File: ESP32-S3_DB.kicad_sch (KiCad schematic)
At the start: 0 parts

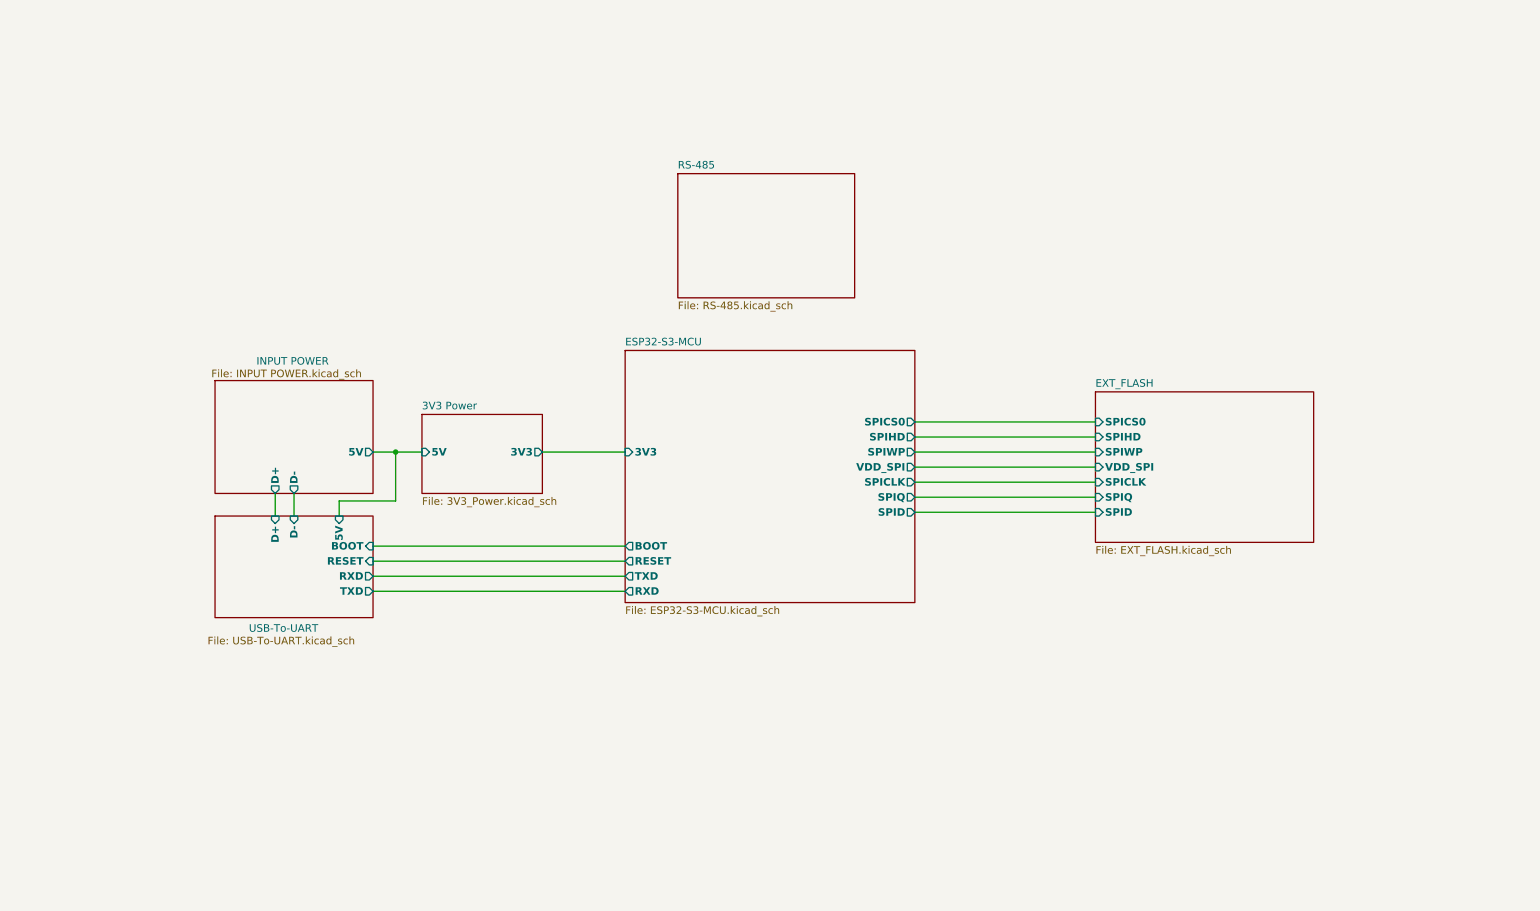
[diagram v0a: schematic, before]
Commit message: Completed RS-485 connections
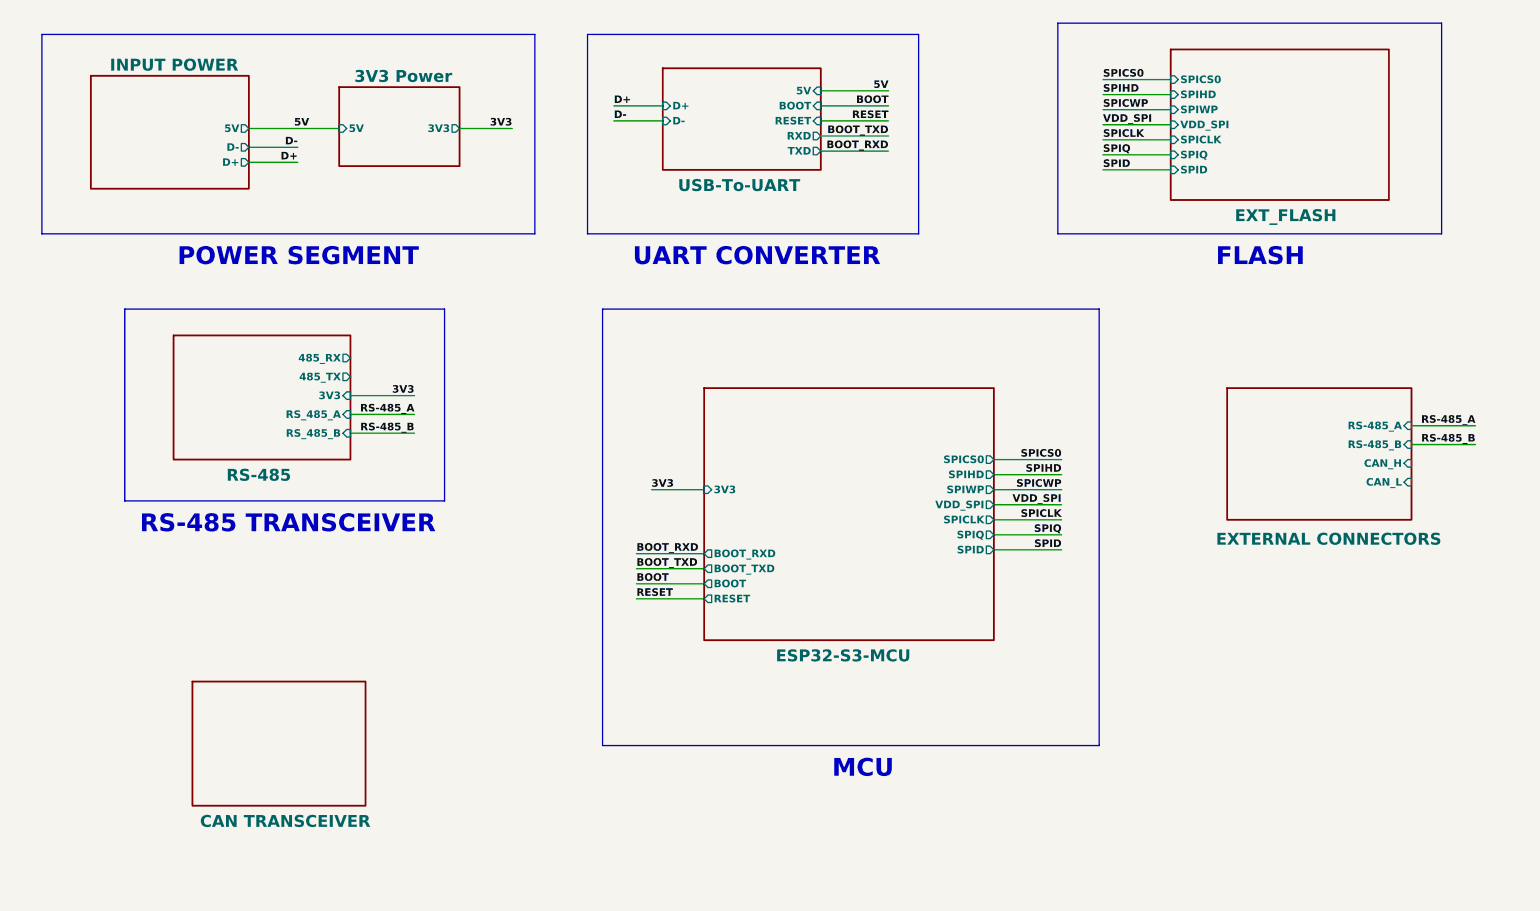
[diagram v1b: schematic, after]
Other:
- added sheet CAN TRANSCEIVER (CAN-TRANSCEIVER.kicad_sch)
- added sheet EXTERNAL CONNECTORS (External_connec.kicad_sch)
- sheet ESP32-S3-MCU ports: added BOOT_RXD, BOOT_TXD; removed RXD, TXD
- sheet RS-485 ports: added 3V3, 485_RX, 485_TX, RS_485_A, RS_485_B; removed none
- note added: "FLASH"
- note added: "MCU"
- note added: "POWER SEGMENT"
- note added: "RS-485 TRANSCEIVER"
- note added: "UART CONVERTER"

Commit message: Added CAN Transceiver
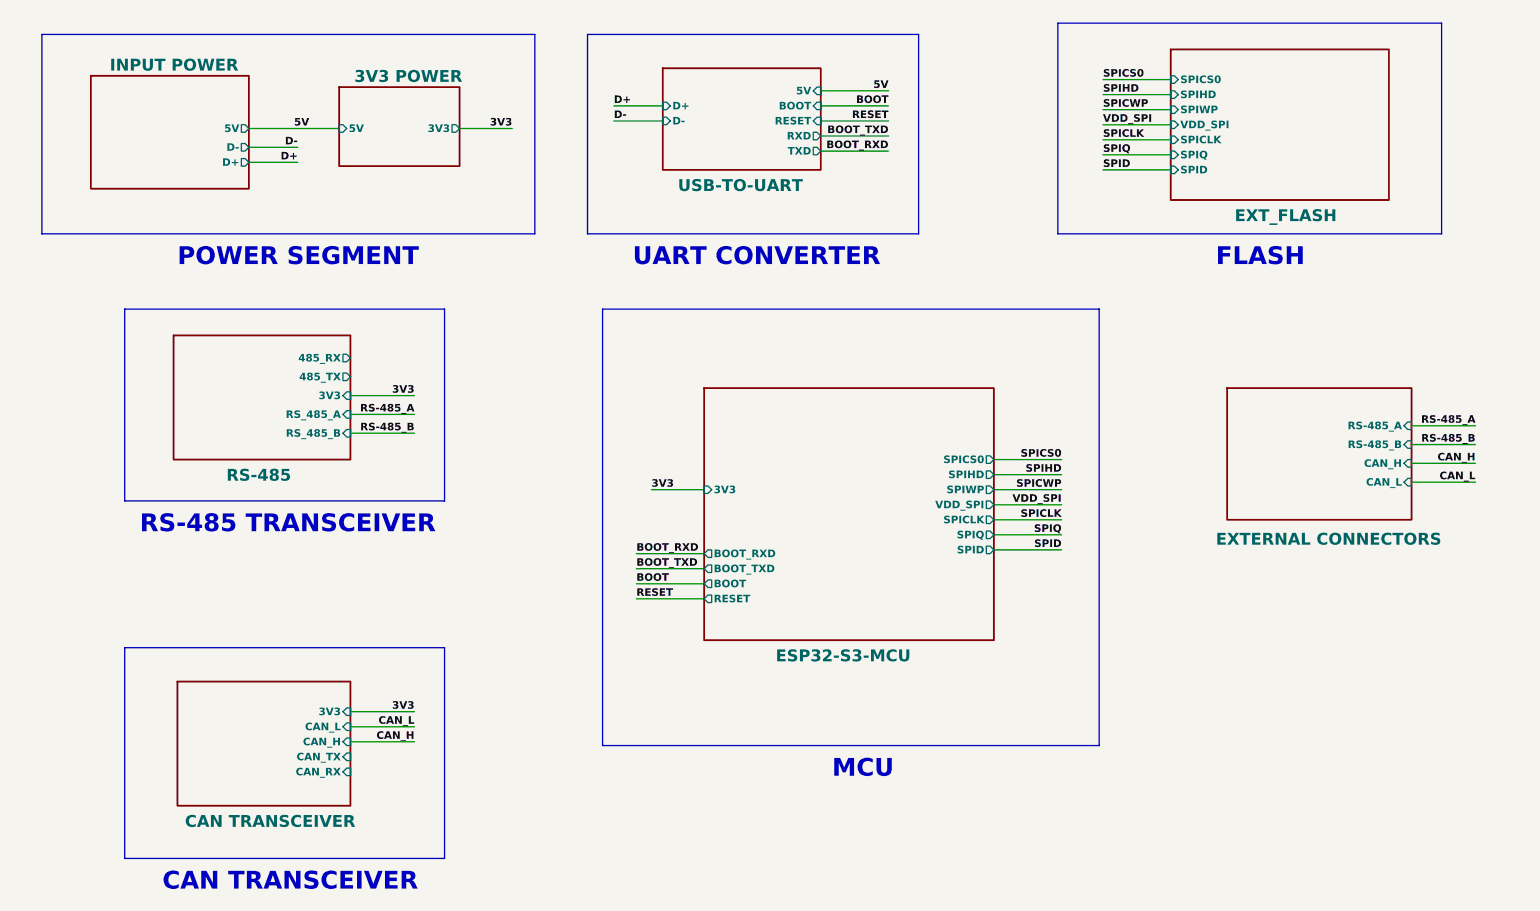
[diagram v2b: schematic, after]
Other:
- sheet 3V3 Power renamed 3V3 POWER
- sheet USB-To-UART renamed USB-TO-UART
- sheet CAN TRANSCEIVER ports: added 3V3, CAN_H, CAN_L, CAN_RX, CAN_TX; removed none
- note added: "CAN TRANSCEIVER"
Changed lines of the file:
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@@
+    (stroke (width 1) (type default) (color 72 72 72 1))
+  )
+  (bus (pts (xy 40.64 125.095) (xy 40.64 160.655))
     (stroke (width 1) (type default) (color 72 72 72 1))
   )
@@
     (stroke (width 1) (type default) (color 72 72 72 1))
   )
+  (wire (pts (xy 78.74 140.97) (xy 89.535 140.97))
+    (stroke (width 0.5) (type default) (color 0 0 0 1))
+  )
   (wire (pts (xy 61.595 43.18) (xy 69.85 43.18))
     (stroke (width 0.5) (type default) (color 0 0 255 1))
@@
   )
   (bus (pts (xy 121.285 67.945) (xy 205.105 67.945))
+    (stroke (width 1) (type default) (color 72 72 72 1))
+  )
+  (bus (pts (xy 40.64 125.095) (xy 94.615 125.095))
     (stroke (width 1) (type default) (color 72 72 72 1))
   )
@@
     (stroke (width 0.5) (type default) (color 255 0 0 1))
   )
+  (bus (pts (xy 94.615 160.655) (xy 40.64 160.655))
+    (stroke (width 1) (type default) (color 72 72 72 1))
+  )
+  (bus (pts (xy 94.615 125.095) (xy 94.615 160.655))
+    (stroke (width 1) (type default) (color 72 72 72 1))
+  )
+  (wire (pts (xy 78.74 138.43) (xy 89.535 138.43))
+    (stroke (width 0.5) (type default) (color 0 0 0 1))
+  )
   (wire (pts (xy 123.19 36.195) (xy 131.445 36.195))
     (stroke (width 0.5) (type default) (color 0 0 255 1))
@@
     (stroke (width 0.5) (type default) (color 0 0 255 1))
   )
+  (wire (pts (xy 257.81 97.155) (xy 268.605 97.155))
+    (stroke (width 0.5) (type default) (color 0 0 0 1))
+  )
+  (wire (pts (xy 78.74 135.89) (xy 89.535 135.89))
+    (stroke (width 0.5) (type default) (color 255 0 0 1))
+  )
   (wire (pts (xy 217.17 39.37) (xy 205.74 39.37))
     (stroke (width 0.5) (type default) (color 0 0 255 1))
@@
   (wire (pts (xy 217.17 36.83) (xy 205.74 36.83))
     (stroke (width 0.5) (type default) (color 0 0 255 1))
+  )
+  (wire (pts (xy 257.81 93.98) (xy 268.605 93.98))
+    (stroke (width 0.5) (type default) (color 0 0 0 1))
   )
   (bus (pts (xy 262.89 55.245) (xy 198.12 55.245))
@@
     (effects (font (size 3 3) bold (color 255 0 0 1)) (justify left bottom))
   )
+  (text "CAN TRANSCEIVER" (at 46.99 166.37 0)
+    (effects (font (size 3 3) bold (color 255 0 0 1)) (justify left bottom))
+  )
   (text "RS-485 TRANSCEIVER" (at 43.18 106.045 0)
     (effects (font (size 3 3) bold (color 255 0 0 1)) (justify left bottom))
@@
     (effects (font (size 1.27 1.27) bold (color 0 0 255 1)) (justify left bottom))
   )
+  (label "3V3" (at 89.535 135.89 180) (fields_autoplaced)
+    (effects (font (size 1.27 1.27) bold (color 255 0 0 1)) (justify right bottom))
+  )
   (label "BOOT_RXD" (at 127 109.22 0) (fields_autoplaced)
     (effects (font (size 1.27 1.27) bold (color 0 0 255 1)) (justify left bottom))
@@
     (effects (font (size 1.27 1.27) bold (color 132 0 0 1)) (justify left bottom))
   )
+  (label "CAN_H" (at 268.605 93.98 180) (fields_autoplaced)
+    (effects (font (size 1.27 1.27) bold (color 0 0 0 1)) (justify right bottom))
+  )
+  (label "CAN_L" (at 268.605 97.155 180) (fields_autoplaced)
+    (effects (font (size 1.27 1.27) bold (color 0 0 0 1)) (justify right bottom))
+  )
   (label "D-" (at 123.19 36.195 0) (fields_autoplaced)
     (effects (font (size 1.27 1.27) bold (color 0 0 255 1)) (justify left bottom))
@@
     (effects (font (size 1.27 1.27) bold (color 0 194 0 1)) (justify left bottom))
   )
+  (label "CAN_H" (at 89.535 140.97 180) (fields_autoplaced)
+    (effects (font (size 1.27 1.27) bold (color 0 0 0 1)) (justify right bottom))
+  )
   (label "SPIQ" (at 198.755 106.045 180) (fields_autoplaced)
     (effects (font (size 1.27 1.27) bold (color 0 0 255 1)) (justify right bottom))
@@
     (effects (font (size 1.27 1.27) bold (color 0 0 255 1)) (justify left bottom))
   )
+  (label "CAN_L" (at 89.535 138.43 180) (fields_autoplaced)
+    (effects (font (size 1.27 1.27) bold (color 0 0 0 1)) (justify right bottom))
+  )
   (sheet (at 217.17 24.13) (size 36.83 25.4)
     (stroke (width 0.3) (type solid) (color 0 0 0 1))
     (fill (color 255 255 194 1.0000))
     (property "Sheetname" "EXT_FLASH" (at 227.965 53.34 0)
-      (effects (font (size 2 2) bold) (justify left bottom))
+      (effects (font (size 2 2) bold (color 0 0 0 1)) (justify left bottom))
     )
     (property "Sheetfile" "EXT_FLASH.kicad_sch" (at 217.17 50.1146 0)
@@
     )
   )
-  (sheet (at 52.07 130.81) (size 29.21 20.955)
-    (stroke (width 0.3) (type solid) (color 0 0 0 1))
-    (fill (color 255 255 194 1.0000))
-    (property "Sheetname" "CAN TRANSCEIVER" (at 53.34 155.575 0)
-      (effects (font (size 2 2) bold) (justify left bottom))
-    )
-    (property "Sheetfile" "CAN-TRANSCEIVER.kicad_sch" (at 52.07 152.4234 0)
-      (effects (font (size 1.27 1.27)) (justify left top) hide)
+  (sheet (at 49.53 130.81) (size 29.21 20.955)
+    (stroke (width 0.3) (type solid) (color 0 0 0 1))
+    (fill (color 255 255 194 1.0000))
+    (property "Sheetname" "CAN TRANSCEIVER" (at 50.8 155.575 0)
+      (effects (font (size 2 2) bold (color 0 0 0 1)) (justify left bottom))
+    )
+    (property "Sheetfile" "CAN-TRANSCEIVER.kicad_sch" (at 49.53 152.4234 0)
+      (effects (font (size 1.27 1.27)) (justify left top) hide)
+    )
+    (pin "CAN_L" input (at 78.74 138.43 0)
+      (effects (font (size 1.27 1.27) (thickness 0.254) bold (color 0 0 0 1)) (justify right))
+    )
+    (pin "3V3" input (at 78.74 135.89 0)
+      (effects (font (size 1.27 1.27) (thickness 0.254) bold (color 255 0 0 1)) (justify right))
+    )
+    (pin "CAN_H" input (at 78.74 140.97 0)
+      (effects (font (size 1.27 1.27) (thickness 0.254) bold (color 0 0 0 1)) (justify right))
+    )
+    (pin "CAN_TX" input (at 78.74 143.51 0)
+      (effects (font (size 1.27 1.27) (thickness 0.254) bold (color 0 0 255 1)) (justify right))
+    )
+    (pin "CAN_RX" input (at 78.74 146.05 0)
+      (effects (font (size 1.27 1.27) (thickness 0.254) bold (color 0 0 255 1)) (justify right))
     )
     (instances
@@
     (fill (color 255 255 194 1.0000))
     (property "Sheetname" "INPUT POWER" (at 38.1 27.94 0)
-      (effects (font (size 2 2) bold) (justify left bottom))
+      (effects (font (size 2 2) bold (color 0 0 0 1)) (justify left bottom))
     )
     (property "Sheetfile" "INPUT POWER.kicad_sch" (at 34.29 48.26 0)
@@
     (fill (color 255 255 194 1.0000))
     (property "Sheetname" "RS-485" (at 57.785 97.155 0)
-      (effects (font (size 2 2) bold) (justify left bottom))
+      (effects (font (size 2 2) bold (color 0 0 0 1)) (justify left bottom))
     )
     (property "Sheetfile" "RS-485.kicad_sch" (at 48.895 93.9296 0)
@@
     (stroke (width 0.3) (type solid) (color 0 0 0 1))
     (fill (color 255 255 194 1.0000))
-    (property "Sheetname" "USB-To-UART" (at 133.985 48.26 0)
-      (effects (font (size 2 2) bold) (justify left bottom))
+    (property "Sheetname" "USB-TO-UART" (at 133.985 48.26 0)
+      (effects (font (size 2 2) bold (color 0 0 0 1)) (justify left bottom))
     )
     (property "Sheetfile" "USB-To-UART.kicad_sch" (at 130.175 47.625 0)
@@
     (fill (color 255 255 194 1.0000))
     (property "Sheetname" "ESP32-S3-MCU" (at 150.495 127.635 0)
-      (effects (font (size 2 2) bold) (justify left bottom))
+      (effects (font (size 2 2) bold (color 0 0 0 1)) (justify left bottom))
     )
     (property "Sheetfile" "ESP32-S3-MCU.kicad_sch" (at 138.43 124.4096 0)
@@
     (fill (color 255 255 194 1.0000))
     (property "Sheetname" "EXTERNAL CONNECTORS" (at 224.79 107.95 0)
-      (effects (font (size 2 2) bold) (justify left bottom))
+      (effects (font (size 2 2) bold (color 0 0 0 1)) (justify left bottom))
     )
     (property "Sheetfile" "External_connec.kicad_sch" (at 226.695 104.0896 0)
@@
     (stroke (width 0.3) (type solid) (color 0 0 0 1))
     (fill (color 255 255 194 1.0000))
-    (property "Sheetname" "3V3 Power" (at 79.375 29.845 0)
-      (effects (font (size 2 2) bold) (justify left bottom))
+    (property "Sheetname" "3V3 POWER" (at 79.375 29.845 0)
+      (effects (font (size 2 2) bold (color 0 0 0 1)) (justify left bottom))
     )
     (property "Sheetfile" "3V3_Power.kicad_sch" (at 75.565 45.085 0)

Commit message: Added IP5306 for power path management
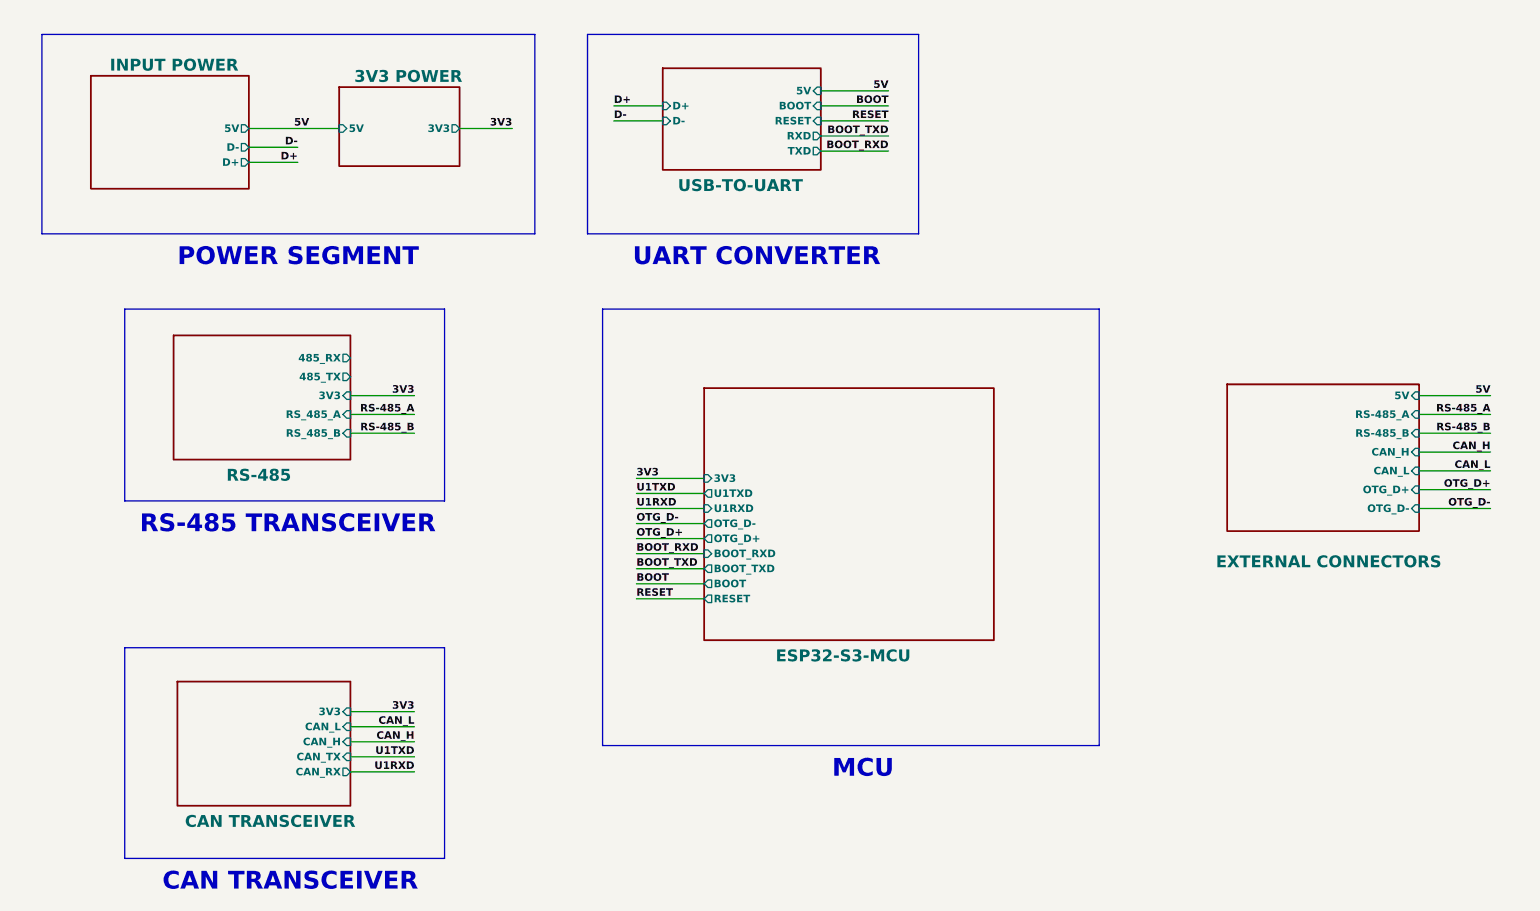
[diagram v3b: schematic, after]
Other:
- removed sheet EXT_FLASH
- sheet ESP32-S3-MCU ports: added OTG_D+, OTG_D-, U1RXD, U1TXD; removed SPICLK, SPICS0, SPID, SPIHD, SPIQ, SPIWP, VDD_SPI
- sheet EXTERNAL CONNECTORS ports: added 5V, OTG_D+, OTG_D-; removed none
- note removed: "FLASH"
